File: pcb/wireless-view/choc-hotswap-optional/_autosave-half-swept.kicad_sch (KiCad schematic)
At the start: 32 parts, among them J1 JST-BATTERY, SW1 SW_Push, SW10 SW_Push, SW11 SW_Push, SW12 SW_Push, SW13 SW_DPDT, SW14 SW_Push, SW15 SW_Push, SW16 SW_Push, SW17 SW_Push, SW18 SW_Push, SW2 SW_Push, SW20 SW_Push, SW21 SW_Push, SW3 SW_Push, SW4 SW_Push, SW5 SW_Push, SW6 SW_Push, SW7 SW_DPDT, SW8 SW_Push, SW9 SW_Push, U1 nice_nano

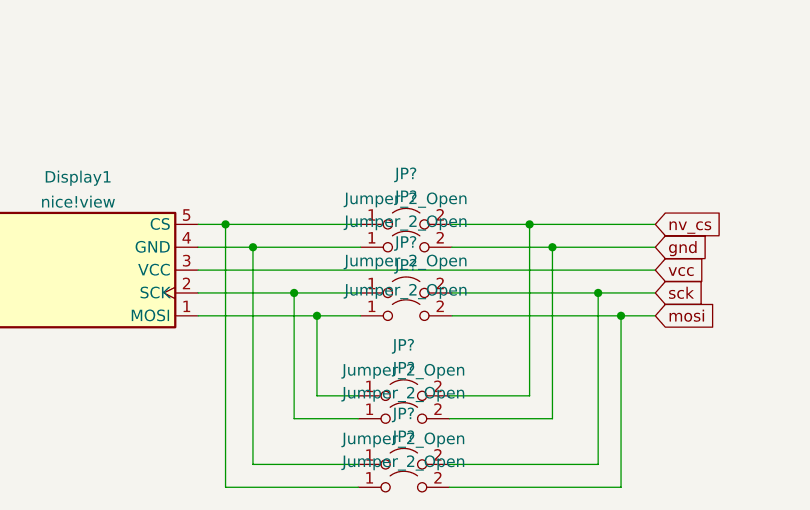
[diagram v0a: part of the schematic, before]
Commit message: made nice view reversible with jumpers, so it's only one footprint now instead of two offset
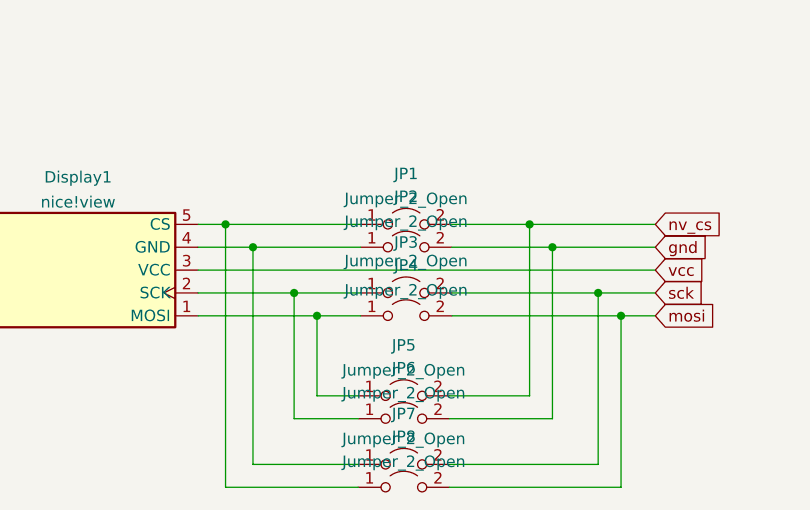
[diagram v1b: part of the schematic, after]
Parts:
- gave numbers to parts that had none: 8
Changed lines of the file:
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@@
   (symbol (lib_id "Jumper:Jumper_2_Open") (at 76.2 162.814 0) (unit 1)
     (in_bom yes) (on_board yes) (fields_autoplaced)
-    (property "Reference" "JP?" (id 0) (at 76.2 157.1965 0))
+    (property "Reference" "JP8" (id 0) (at 76.2 157.1965 0))
     (property "Value" "Jumper_2_Open" (id 1) (at 76.2 159.9716 0))
     (property "Footprint" "Jumper:SolderJumper-2_P1.3mm_Open_TrianglePad1.0x1.5mm" (id 2) (at 76.2 162.814 0)
@@
   (symbol (lib_id "Jumper:Jumper_2_Open") (at 76.454 136.144 0) (unit 1)
     (in_bom yes) (on_board yes) (fields_autoplaced)
-    (property "Reference" "JP?" (id 0) (at 76.454 130.5265 0))
+    (property "Reference" "JP2" (id 0) (at 76.454 130.5265 0))
     (property "Value" "Jumper_2_Open" (id 1) (at 76.454 133.3016 0))
     (property "Footprint" "Jumper:SolderJumper-2_P1.3mm_Open_TrianglePad1.0x1.5mm" (id 2) (at 76.454 136.144 0)
@@
   (symbol (lib_id "Jumper:Jumper_2_Open") (at 76.454 133.604 0) (unit 1)
     (in_bom yes) (on_board yes) (fields_autoplaced)
-    (property "Reference" "JP?" (id 0) (at 76.454 127.9865 0))
+    (property "Reference" "JP1" (id 0) (at 76.454 127.9865 0))
     (property "Value" "Jumper_2_Open" (id 1) (at 76.454 130.7616 0))
     (property "Footprint" "Jumper:SolderJumper-2_P1.3mm_Open_TrianglePad1.0x1.5mm" (id 2) (at 76.454 133.604 0)
@@
   (symbol (lib_id "Jumper:Jumper_2_Open") (at 76.2 152.654 0) (unit 1)
     (in_bom yes) (on_board yes) (fields_autoplaced)
-    (property "Reference" "JP?" (id 0) (at 76.2 147.0365 0))
+    (property "Reference" "JP5" (id 0) (at 76.2 147.0365 0))
     (property "Value" "Jumper_2_Open" (id 1) (at 76.2 149.8116 0))
     (property "Footprint" "Jumper:SolderJumper-2_P1.3mm_Open_TrianglePad1.0x1.5mm" (id 2) (at 76.2 152.654 0)
@@
   (symbol (lib_id "Jumper:Jumper_2_Open") (at 76.454 143.764 0) (unit 1)
     (in_bom yes) (on_board yes) (fields_autoplaced)
-    (property "Reference" "JP?" (id 0) (at 76.454 138.1465 0))
+    (property "Reference" "JP4" (id 0) (at 76.454 138.1465 0))
     (property "Value" "Jumper_2_Open" (id 1) (at 76.454 140.9216 0))
     (property "Footprint" "Jumper:SolderJumper-2_P1.3mm_Open_TrianglePad1.0x1.5mm" (id 2) (at 76.454 143.764 0)
@@
   (symbol (lib_id "Jumper:Jumper_2_Open") (at 76.454 141.224 0) (unit 1)
     (in_bom yes) (on_board yes)
-    (property "Reference" "JP?" (id 0) (at 76.454 135.6065 0))
+    (property "Reference" "JP3" (id 0) (at 76.454 135.6065 0))
     (property "Value" "Jumper_2_Open" (id 1) (at 76.454 137.668 0))
     (property "Footprint" "Jumper:SolderJumper-2_P1.3mm_Open_TrianglePad1.0x1.5mm" (id 2) (at 76.454 141.224 0)
@@
   (symbol (lib_id "Jumper:Jumper_2_Open") (at 76.2 160.274 0) (unit 1)
     (in_bom yes) (on_board yes) (fields_autoplaced)
-    (property "Reference" "JP?" (id 0) (at 76.2 154.6565 0))
+    (property "Reference" "JP7" (id 0) (at 76.2 154.6565 0))
     (property "Value" "Jumper_2_Open" (id 1) (at 76.2 157.4316 0))
     (property "Footprint" "Jumper:SolderJumper-2_P1.3mm_Open_TrianglePad1.0x1.5mm" (id 2) (at 76.2 160.274 0)
@@
   (symbol (lib_id "Jumper:Jumper_2_Open") (at 76.2 155.194 0) (unit 1)
     (in_bom yes) (on_board yes) (fields_autoplaced)
-    (property "Reference" "JP?" (id 0) (at 76.2 149.5765 0))
+    (property "Reference" "JP6" (id 0) (at 76.2 149.5765 0))
     (property "Value" "Jumper_2_Open" (id 1) (at 76.2 152.3516 0))
     (property "Footprint" "Jumper:SolderJumper-2_P1.3mm_Open_TrianglePad1.0x1.5mm" (id 2) (at 76.2 155.194 0)
@@
       (reference "J1") (unit 1) (value "JST-BATTERY") (footprint "Connector_JST:JST_PH_S3B-PH-K_1x03_P2.00mm_Horizontal")
     )
+    (path "/9e675945-b3ef-45fc-b0c0-ae7d5196314f"
+      (reference "JP1") (unit 1) (value "Jumper_2_Open") (footprint "Jumper:SolderJumper-2_P1.3mm_Open_TrianglePad1.0x1.5mm")
+    )
+    (path "/467f624c-97ea-450a-8a29-84010edf11b2"
+      (reference "JP2") (unit 1) (value "Jumper_2_Open") (footprint "Jumper:SolderJumper-2_P1.3mm_Open_TrianglePad1.0x1.5mm")
+    )
+    (path "/cf11df2f-d54e-43bb-aae6-bcc998f1ace1"
+      (reference "JP3") (unit 1) (value "Jumper_2_Open") (footprint "Jumper:SolderJumper-2_P1.3mm_Open_TrianglePad1.0x1.5mm")
+    )
+    (path "/c5f462c4-5085-48e6-be04-f1c472750918"
+      (reference "JP4") (unit 1) (value "Jumper_2_Open") (footprint "Jumper:SolderJumper-2_P1.3mm_Open_TrianglePad1.0x1.5mm")
+    )
+    (path "/9f81a0ad-91a9-4222-a816-8428cdcec98c"
+      (reference "JP5") (unit 1) (value "Jumper_2_Open") (footprint "Jumper:SolderJumper-2_P1.3mm_Open_TrianglePad1.0x1.5mm")
+    )
+    (path "/f767c241-0d2a-4a60-af21-e950fbb9f412"
+      (reference "JP6") (unit 1) (value "Jumper_2_Open") (footprint "Jumper:SolderJumper-2_P1.3mm_Open_TrianglePad1.0x1.5mm")
+    )
+    (path "/d1900729-d56b-4976-aa55-9cc260dc60e7"
+      (reference "JP7") (unit 1) (value "Jumper_2_Open") (footprint "Jumper:SolderJumper-2_P1.3mm_Open_TrianglePad1.0x1.5mm")
+    )
     (path "/0b93f6f6-8a82-473c-8f29-17cf3f741034"
-      (reference "JP?") (unit 1) (value "Jumper_2_Open") (footprint "Jumper:SolderJumper-2_P1.3mm_Open_TrianglePad1.0x1.5mm")
-    )
-    (path "/467f624c-97ea-450a-8a29-84010edf11b2"
-      (reference "JP?") (unit 1) (value "Jumper_2_Open") (footprint "Jumper:SolderJumper-2_P1.3mm_Open_TrianglePad1.0x1.5mm")
-    )
-    (path "/9e675945-b3ef-45fc-b0c0-ae7d5196314f"
-      (reference "JP?") (unit 1) (value "Jumper_2_Open") (footprint "Jumper:SolderJumper-2_P1.3mm_Open_TrianglePad1.0x1.5mm")
-    )
-    (path "/9f81a0ad-91a9-4222-a816-8428cdcec98c"
-      (reference "JP?") (unit 1) (value "Jumper_2_Open") (footprint "Jumper:SolderJumper-2_P1.3mm_Open_TrianglePad1.0x1.5mm")
-    )
-    (path "/c5f462c4-5085-48e6-be04-f1c472750918"
-      (reference "JP?") (unit 1) (value "Jumper_2_Open") (footprint "Jumper:SolderJumper-2_P1.3mm_Open_TrianglePad1.0x1.5mm")
-    )
-    (path "/cf11df2f-d54e-43bb-aae6-bcc998f1ace1"
-      (reference "JP?") (unit 1) (value "Jumper_2_Open") (footprint "Jumper:SolderJumper-2_P1.3mm_Open_TrianglePad1.0x1.5mm")
-    )
-    (path "/d1900729-d56b-4976-aa55-9cc260dc60e7"
-      (reference "JP?") (unit 1) (value "Jumper_2_Open") (footprint "Jumper:SolderJumper-2_P1.3mm_Open_TrianglePad1.0x1.5mm")
-    )
-    (path "/f767c241-0d2a-4a60-af21-e950fbb9f412"
-      (reference "JP?") (unit 1) (value "Jumper_2_Open") (footprint "Jumper:SolderJumper-2_P1.3mm_Open_TrianglePad1.0x1.5mm")
+      (reference "JP8") (unit 1) (value "Jumper_2_Open") (footprint "Jumper:SolderJumper-2_P1.3mm_Open_TrianglePad1.0x1.5mm")
     )
     (path "/00000000-0000-0000-0000-0000604ea4f3"
